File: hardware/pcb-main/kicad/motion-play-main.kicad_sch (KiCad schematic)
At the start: 26 parts, among them J2 DWEII Power Module, J3 LED_Strip, J4 Conn_01x05, J5 Conn_01x05, J6 Conn_01x05, U1 AP2112K-3.3TRG1, U2 T-Display-S3

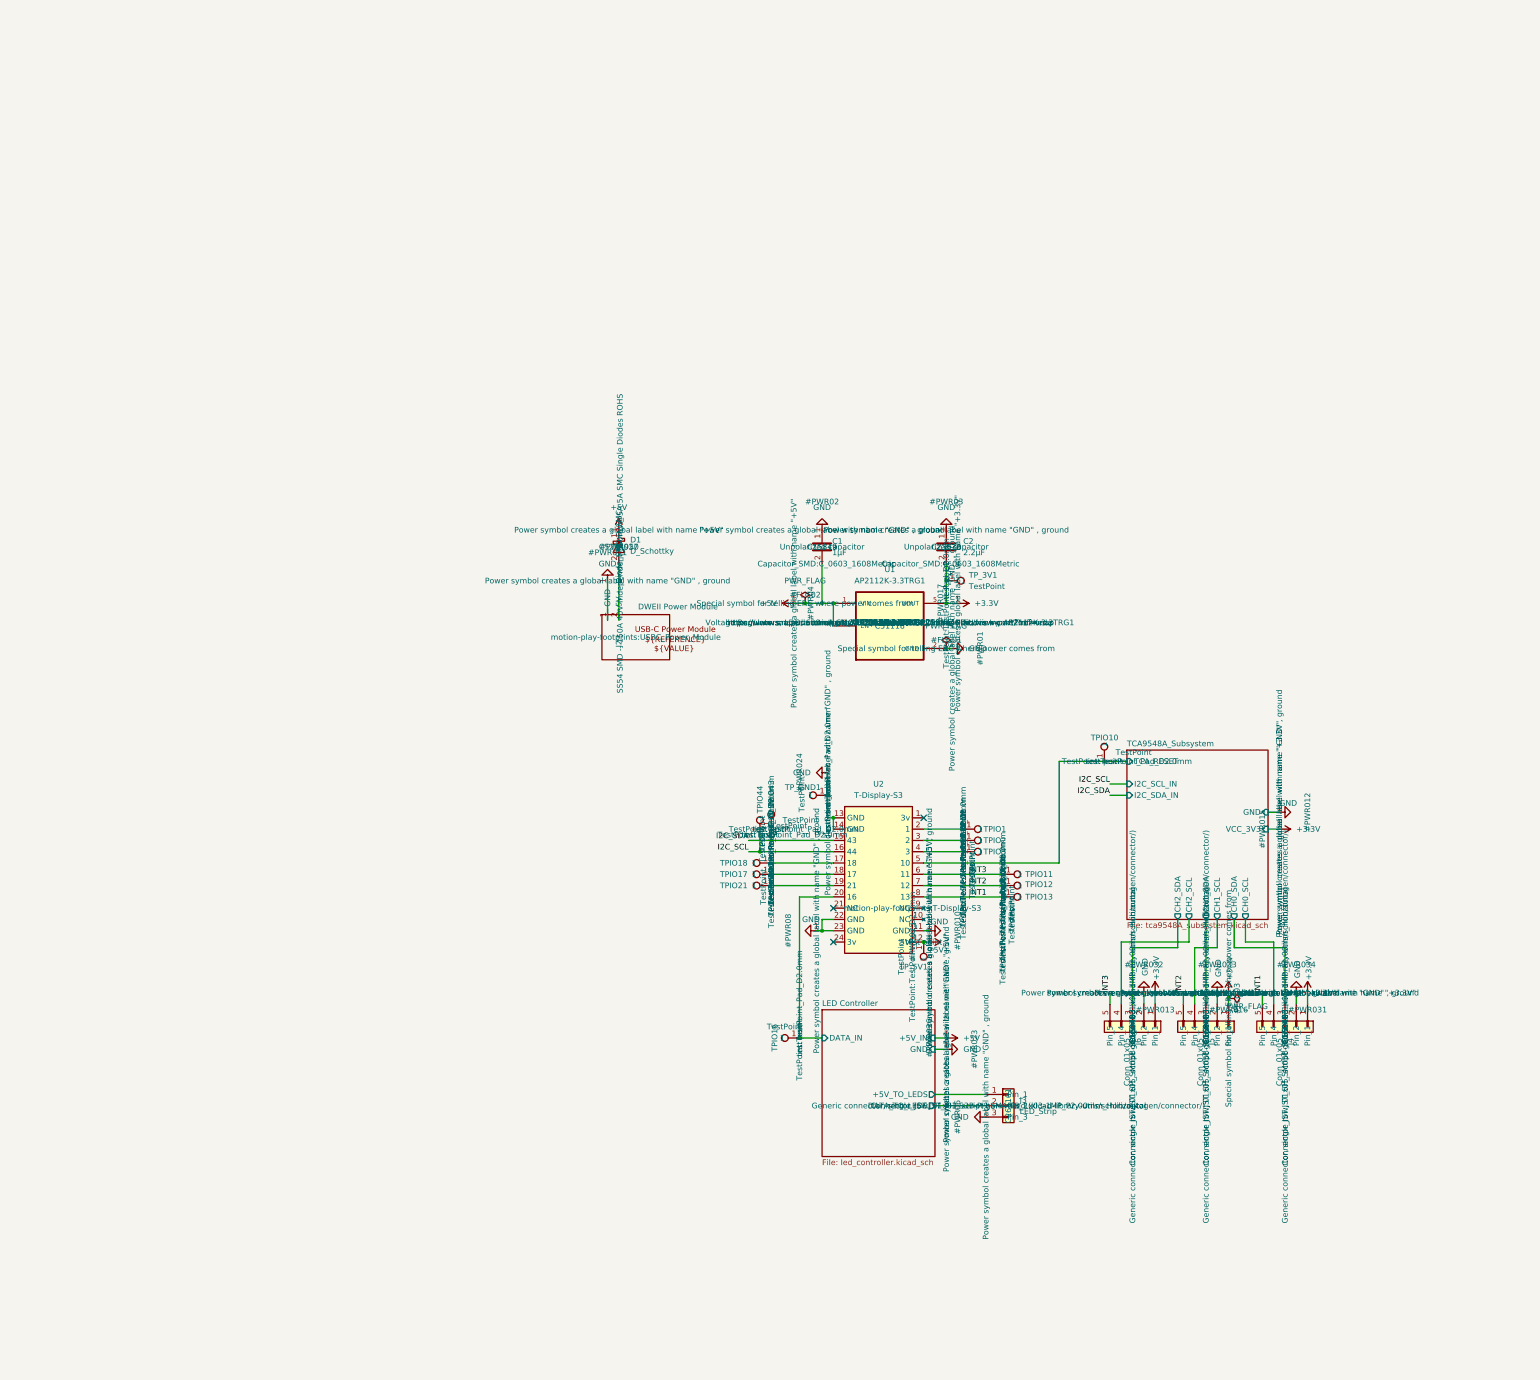
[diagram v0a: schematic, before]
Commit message: Integrate power management sub-sheet into root schematic (Phase 3.6)
- Delete J2 (DWEII USB-C module) and D1 (Schottky) from root sheet
- Add hierarchical sheet reference to power_management.kicad_sch
- Wire 6 sheet pins: +5V, GND, +3.3V, I2C_SDA, I2C_SCL, CHRG_INT
- Connect CHRG_INT to GPIO 21 (U2 pin 19)
- Hide non-essential property labels (Description, Datasheet, etc.)
  across all original schematic sheets — only Reference and Value visible
- ERC: 0 errors on root/LED/TCA9548A sheets, 4 expected power_pin
  warnings on power management sheet (net labels vs PWR_FLAG)

Made-with: Cursor
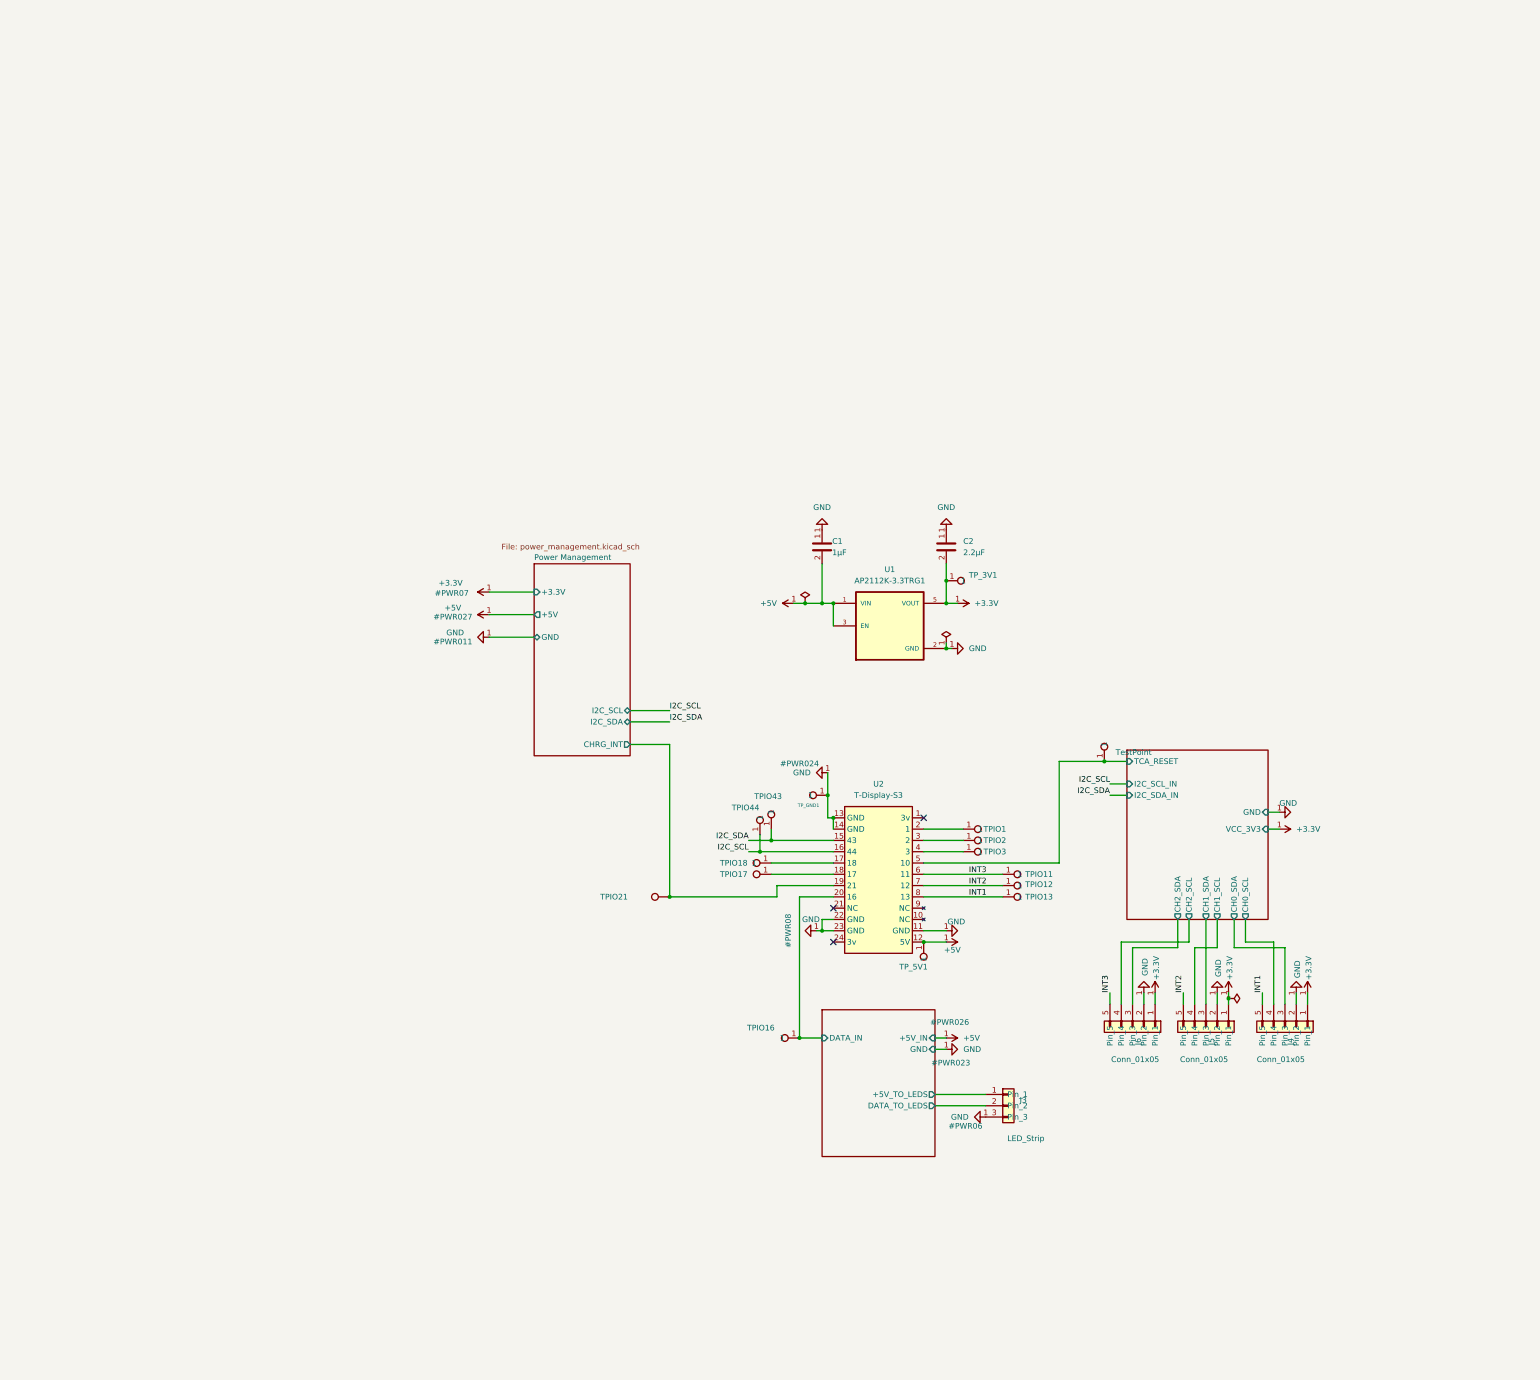
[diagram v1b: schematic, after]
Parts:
- removed D1: D_Schottky, Diode_SMD:D_SMC, symbol Device:D_Schottky
- removed J2: DWEII Power Module, motion-play-footprints:USBC_Power_Module, symbol motion-play-symbols:USBC_Power_Module
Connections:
- net Power Management/CHRG_INT: now reaches TPIO21.1, U2.19 (21)
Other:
- added sheet Power Management (power_management.kicad_sch)

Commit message: Add AI annotations and context review for power management components (Phase 4)
Phase 4 of integrated power initiative: extracted circuit-context.json with
all 55 new power management components, performed pin-by-pin review against
spec with zero discrepancies, and wrote AI annotations for all 51 physical
components plus updated TPIO21 (GPIO 21 now CHRG_INT). 86/86 components
annotated (100% coverage). Added 6 block definitions, annotated 26 nets,
and updated stale descriptions from pre-power-management era.

Made-with: Cursor
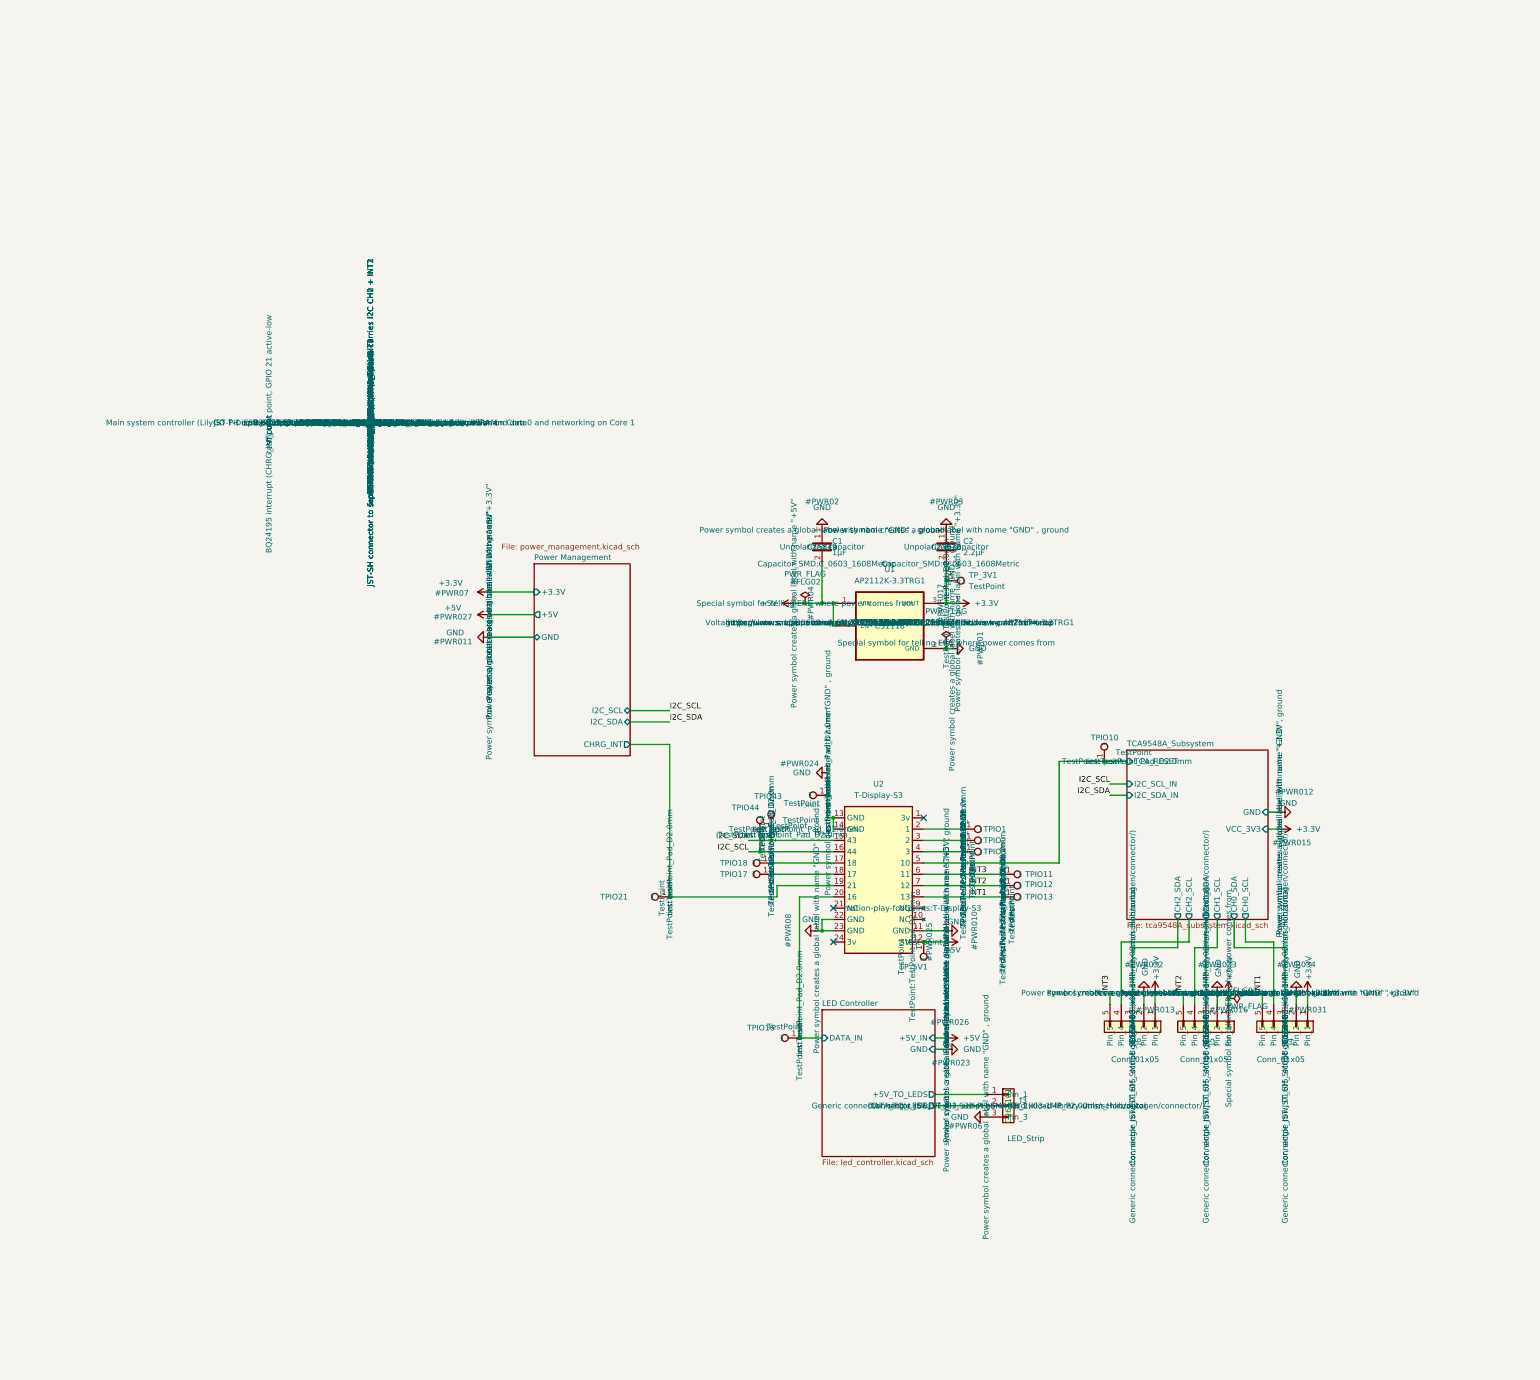
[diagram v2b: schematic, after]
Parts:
- TPIO21: ai_function GPIO 21 breakout test point (unused) -> BQ24195 interrupt (CHRG_INT) test point, GPIO 21 active-low

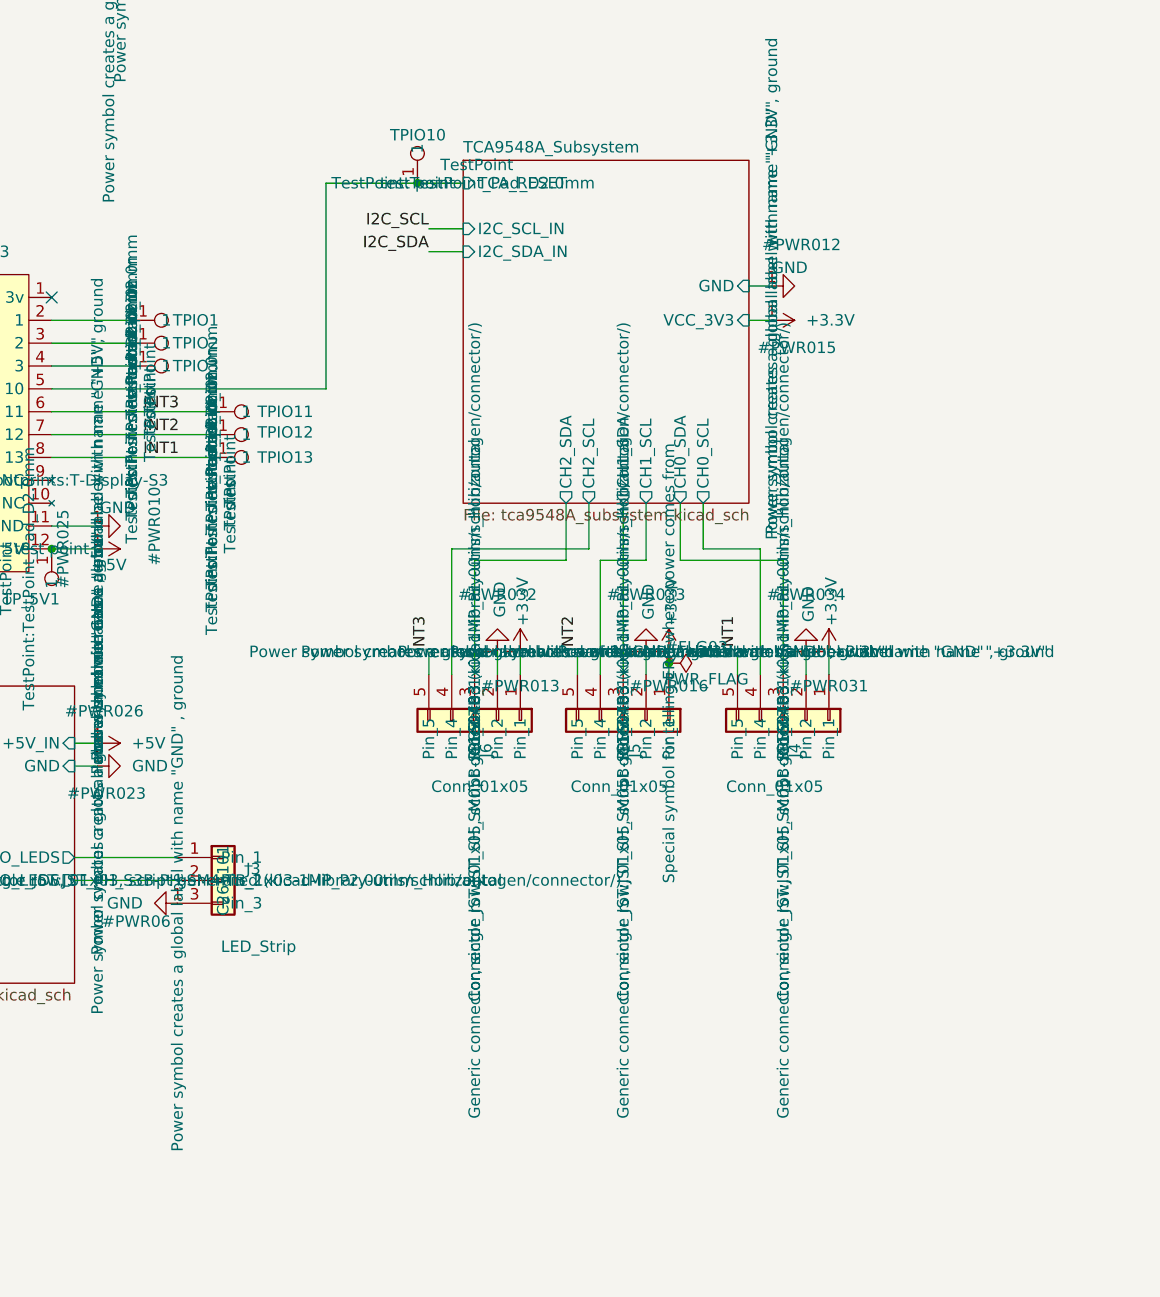
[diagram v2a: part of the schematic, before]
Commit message: Fix L2 bbox, re-place power components, complete full board routing
- Fix extract.py inductor bbox heuristic: parse L{X}-W{Y} from footprint
  name when pad-based bbox height < width/2 (L2: 8.4×3.2 → 8.4×6.6mm)
- Add L2 to placement anchors, re-run placement pushing C32/R41/R42/R43/TP4
  out of L2's physical footprint
- Fix J7 USB-C schematic pin-to-footprint mapping (A4→A4B9, etc.)
- Complete all trace routing: power switching loops (BOOST_SW pour, BQ_SW),
  VSYS/VBAT/Protected_VBUS power paths, INA219 Kelvin sense, +5V distribution
  via In2.Cu zone, I2C bus, all U5/U6 support passives
- Board setup: net classes, design rules, zone fills
- DRC: 0 unconnected pads, remaining violations are easyeda2kicad footprint
  artifacts (U6 thermal vias, J7 pad spacing) and expected tight QFN escapes

Made-with: Cursor
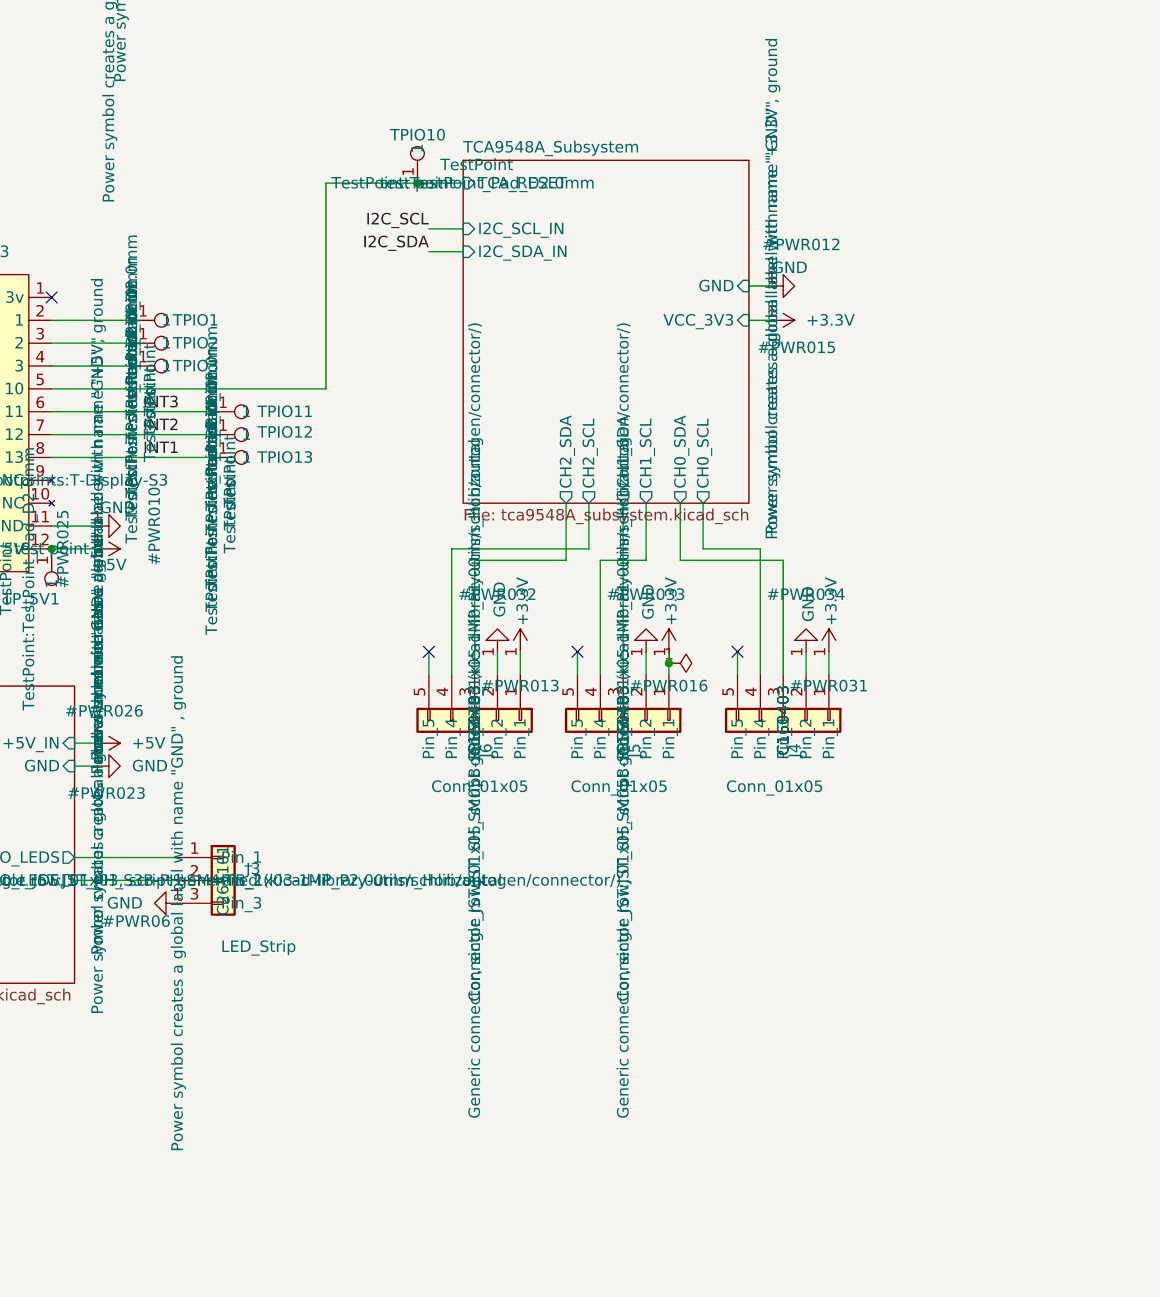
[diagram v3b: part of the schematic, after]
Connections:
- net INT1: no longer J4.5 (Pin_5)
- net INT2: no longer J5.5 (Pin_5)
- net INT3: no longer J6.5 (Pin_5)
- no-connect marks 3 -> 6
